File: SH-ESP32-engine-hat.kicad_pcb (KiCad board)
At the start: 2 copper layers, 34 x 58 mm, 66 parts, among them J301 I2C_top, J302 I2C_bottom, J303 GPIO subset, J304 Opto_bottom, J305 1-Wire_top, J306 1-Wire_bottom, J307 Opto_top, J401 Conn_01x02, J402 Conn_01x02, J501 Conn_01x02, J601 Alarm input, Q401 S9015, Q402 S9015, U401 LMV324, U402 RCLAMP0524P-N, U403 RCLAMP0524P-N, U601 ELQ3H7

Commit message: Make all TH headers virtual
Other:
- board text added: "JLCJLCJLCJLC"

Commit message: Fix the footprint for ELQ3H7
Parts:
- U601: footprint Package_SO:SOIC-16W_5.3x10.2mm_P1.27mm -> Package_SO:SOIC-16_4.55x10.3mm_P1.27mm
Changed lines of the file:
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@@
     (add_net "Net-(D603-Pad1)")
     (add_net "Net-(D604-Pad1)")
+    (add_net "Net-(J303-Pad1)")
+    (add_net "Net-(J303-Pad11)")
+    (add_net "Net-(J303-Pad13)")
+    (add_net "Net-(J303-Pad3)")
+    (add_net "Net-(J303-Pad5)")
+    (add_net "Net-(J303-Pad7)")
     (add_net "Net-(J501-Pad2)")
     (add_net "Net-(Q401-Pad1)")
@@
     (add_net "Net-(Q402-Pad1)")
     (add_net "Net-(Q402-Pad2)")
-  )
-  (module SH-ESP32-tank-hat:HL_pictogram_6.3mm (layer F.Cu)
+    (add_net "Net-(U401-Pad14)")
+    (add_net "Net-(U401-Pad8)")
+    (add_net "Net-(U402-Pad2)")
+    (add_net "Net-(U402-Pad4)")
+    (add_net "Net-(U402-Pad5)")
+    (add_net "Net-(U402-Pad6)")
+    (add_net "Net-(U402-Pad7)")
+    (add_net "Net-(U402-Pad9)")
+    (add_net "Net-(U403-Pad2)")
+    (add_net "Net-(U403-Pad4)")
+    (add_net "Net-(U403-Pad5)")
+    (add_net "Net-(U403-Pad6)")
+    (add_net "Net-(U403-Pad7)")
+    (add_net "Net-(U403-Pad9)")
+  )
+  (module Package_SO:SOIC-16_4.55x10.3mm_P1.27mm (layer F.Cu)
+    (at 132.1 73.8 90)
+    (descr "SOIC, 16 Pin (https://toshiba.semicon-storage.com/info/docget.jsp?did=12858&prodName=TLP291-4), generated with kicad-footprint-generator ipc_gullwing_generator.py")
+    (tags "SOIC SO")
+    (attr smd)
+    (fp_text reference U601 (at 0 -6.1 90) (layer F.SilkS) hide
+      (effects (font (size 1 1) (thickness 0.15)))
+    )
+    (fp_text value ELQ3H7 (at 0 6.1 90) (layer F.Fab) hide
+      (effects (font (size 1 1) (thickness 0.15)))
+    )
+    (fp_text user %R (at 0 0 90) (layer F.Fab) hide
+      (effects (font (size 1 1) (thickness 0.15)))
+    )
+    (fp_line (start 0 5.26) (end 2.385 5.26) (layer F.SilkS) (width 0.12))
+    (fp_line (start 2.385 5.26) (end 2.385 4.98) (layer F.SilkS) (width 0.12))
+    (fp_line (start 0 5.26) (end -2.385 5.26) (layer F.SilkS) (width 0.12))
+    (fp_line (start -2.385 5.26) (end -2.385 4.98) (layer F.SilkS) (width 0.12))
+    (fp_line (start 0 -5.26) (end 2.385 -5.26) (layer F.SilkS) (width 0.12))
+    (fp_line (start 2.385 -5.26) (end 2.385 -4.98) (layer F.SilkS) (width 0.12))
+    (fp_line (start 0 -5.26) (end -2.385 -5.26) (layer F.SilkS) (width 0.12))
+    (fp_line (start -2.385 -5.26) (end -2.385 -4.98) (layer F.SilkS) (width 0.12))
+    (fp_line (start -2.385 -4.98) (end -4.05 -4.98) (layer F.SilkS) (width 0.12))
+    (fp_line (start -1.275 -5.15) (end 2.275 -5.15) (layer F.Fab) (width 0.1))
+    (fp_line (start 2.275 -5.15) (end 2.275 5.15) (layer F.Fab) (width 0.1))
+    (fp_line (start 2.275 5.15) (end -2.275 5.15) (layer F.Fab) (width 0.1))
+    (fp_line (start -2.275 5.15) (end -2.275 -4.15) (layer F.Fab) (width 0.1))
+    (fp_line (start -2.275 -4.15) (end -1.275 -5.15) (layer F.Fab) (width 0.1))
+    (fp_line (start -4.3 -5.4) (end -4.3 5.4) (layer F.CrtYd) (width 0.05))
+    (fp_line (start -4.3 5.4) (end 4.3 5.4) (layer F.CrtYd) (width 0.05))
+    (fp_line (start 4.3 5.4) (end 4.3 -5.4) (layer F.CrtYd) (width 0.05))
+    (fp_line (start 4.3 -5.4) (end -4.3 -5.4) (layer F.CrtYd) (width 0.05))
+    (pad 16 smd roundrect (at 3.25 -4.445 90) (size 1.6 0.55) (layers F.Cu F.Paste F.Mask) (roundrect_rratio 0.25)
+      (net 2 +3V3))
+    (pad 15 smd roundrect (at 3.25 -3.175 90) (size 1.6 0.55) (layers F.Cu F.Paste F.Mask) (roundrect_rratio 0.25)
+      (net 38 /AL1))
+    (pad 14 smd roundrect (at 3.25 -1.905 90) (size 1.6 0.55) (layers F.Cu F.Paste F.Mask) (roundrect_rratio 0.25)
+      (net 2 +3V3))
+    (pad 13 smd roundrect (at 3.25 -0.635 90) (size 1.6 0.55) (layers F.Cu F.Paste F.Mask) (roundrect_rratio 0.25)
+      (net 37 /AL2))
+    (pad 12 smd roundrect (at 3.25 0.635 90) (size 1.6 0.55) (layers F.Cu F.Paste F.Mask) (roundrect_rratio 0.25)
+      (net 2 +3V3))
+    (pad 11 smd roundrect (at 3.25 1.905 90) (size 1.6 0.55) (layers F.Cu F.Paste F.Mask) (roundrect_rratio 0.25)
+      (net 36 /AL3))
+    (pad 10 smd roundrect (at 3.25 3.175 90) (size 1.6 0.55) (layers F.Cu F.Paste F.Mask) (roundrect_rratio 0.25)
+      (net 2 +3V3))
+    (pad 9 smd roundrect (at 3.25 4.445 90) (size 1.6 0.55) (layers F.Cu F.Paste F.Mask) (roundrect_rratio 0.25)
+      (net 35 /AL4))
+    (pad 8 smd roundrect (at -3.25 4.445 90) (size 1.6 0.55) (layers F.Cu F.Paste F.Mask) (roundrect_rratio 0.25)
+      (net 29 "/Optocoupler input/GND4"))
+    (pad 7 smd roundrect (at -3.25 3.175 90) (size 1.6 0.55) (layers F.Cu F.Paste F.Mask) (roundrect_rratio 0.25)
+      (net 27 "Net-(D604-Pad1)"))
+    (pad 6 smd roundrect (at -3.25 1.905 90) (size 1.6 0.55) (layers F.Cu F.Paste F.Mask) (roundrect_rratio 0.25)
+      (net 30 "/Optocoupler input/GND3"))
+    (pad 5 smd roundrect (at -3.25 0.635 90) (size 1.6 0.55) (layers F.Cu F.Paste F.Mask) (roundrect_rratio 0.25)
+      (net 25 "Net-(D603-Pad1)"))
+    (pad 4 smd roundrect (at -3.25 -0.635 90) (size 1.6 0.55) (layers F.Cu F.Paste F.Mask) (roundrect_rratio 0.25)
+      (net 31 "/Optocoupler input/GND2"))
+    (pad 3 smd roundrect (at -3.25 -1.905 90) (size 1.6 0.55) (layers F.Cu F.Paste F.Mask) (roundrect_rratio 0.25)
+      (net 23 "Net-(D602-Pad1)"))
+    (pad 2 smd roundrect (at -3.25 -3.175 90) (size 1.6 0.55) (layers F.Cu F.Paste F.Mask) (roundrect_rratio 0.25)
+      (net 32 "/Optocoupler input/GND1"))
+    (pad 1 smd roundrect (at -3.25 -4.445 90) (size 1.6 0.55) (layers F.Cu F.Paste F.Mask) (roundrect_rratio 0.25)
+      (net 21 "Net-(D601-Pad1)"))
+    (model ${KISYS3DMOD}/Package_SO.3dshapes/SOIC-16_4.55x10.3mm_P1.27mm.wrl
+      (at (xyz 0 0 0))
+      (scale (xyz 1 1 1))
+      (rotate (xyz 0 0 0))
+    )
+  )
+  (module SH-ESP32-tank-hat:HL_pictogram_6.3mm locked (layer F.Cu)
     (at 145.2 94.7)
     (fp_text reference G*** (at 0 0) (layer F.SilkS) hide
@@
       (xy -0.095909 -3.166816) (xy 0.183489 -3.163253)) (layer F.SilkS) (width 0.01))
   )
-  (module SH-ESP32-tank-hat:Hat_Labs_20mm (layer B.Cu)
+  (module SH-ESP32-tank-hat:Hat_Labs_20mm locked (layer B.Cu)
     (at 149.3 94.9 180)
     (fp_text reference G*** (at 0 0) (layer B.SilkS) hide
@@
       (at (xyz 0 0 0))
       (scale (xyz 1 1 1))
-      (rotate (xyz 0 0 0))
-    )
-  )
-  (module Package_SO:SOIC-16W_5.3x10.2mm_P1.27mm (layer F.Cu)
-    (at 132.1 73.8 90)
-    (descr "16-Lead Plastic Small Outline (SO) - Wide, 5.3 mm Body (http://www.ti.com/lit/ml/msop002a/msop002a.pdf)")
-    (tags "SOIC 1.27")
-    (attr smd)
-    (fp_text reference U601 (at 0 -6.2 90) (layer F.SilkS) hide
-      (effects (font (size 1 1) (thickness 0.15)))
-    )
-    (fp_text value ELQ3H7 (at 0 6.2 90) (layer F.Fab) hide
-      (effects (font (size 1 1) (thickness 0.15)))
-    )
-    (fp_line (start -2.775 -5) (end -4.3 -5) (layer F.SilkS) (width 0.15))
-    (fp_line (start -2.775 5.275) (end 2.775 5.275) (layer F.SilkS) (width 0.15))
-    (fp_line (start -2.775 -5.275) (end 2.775 -5.275) (layer F.SilkS) (width 0.15))
-    (fp_line (start -2.775 5.275) (end -2.775 4.92) (layer F.SilkS) (width 0.15))
-    (fp_line (start 2.775 5.275) (end 2.775 4.92) (layer F.SilkS) (width 0.15))
-    (fp_line (start 2.775 -5.275) (end 2.775 -4.92) (layer F.SilkS) (width 0.15))
-    (fp_line (start -2.775 -5.275) (end -2.775 -5) (layer F.SilkS) (width 0.15))
-    (fp_line (start -4.55 5.45) (end 4.55 5.45) (layer F.CrtYd) (width 0.05))
-    (fp_line (start -4.55 -5.45) (end 4.55 -5.45) (layer F.CrtYd) (width 0.05))
-    (fp_line (start 4.55 -5.45) (end 4.55 5.45) (layer F.CrtYd) (width 0.05))
-    (fp_line (start -4.55 -5.45) (end -4.55 5.45) (layer F.CrtYd) (width 0.05))
-    (fp_line (start -2.65 -4.1) (end -1.65 -5.1) (layer F.Fab) (width 0.15))
-    (fp_line (start -2.65 5.1) (end -2.65 -4.1) (layer F.Fab) (width 0.15))
-    (fp_line (start 2.65 5.1) (end -2.65 5.1) (layer F.Fab) (width 0.15))
-    (fp_line (start 2.65 -5.1) (end 2.65 5.1) (layer F.Fab) (width 0.15))
-    (fp_line (start -1.65 -5.1) (end 2.65 -5.1) (layer F.Fab) (width 0.15))
-    (fp_text user %R (at 0 0 90) (layer F.Fab) hide
-      (effects (font (size 1 1) (thickness 0.15)))
-    )
-    (pad 16 smd rect (at 3.55 -4.445 90) (size 1.5 0.6) (layers F.Cu F.Paste F.Mask)
-      (net 2 +3V3))
-    (pad 15 smd rect (at 3.55 -3.175 90) (size 1.5 0.6) (layers F.Cu F.Paste F.Mask)
-      (net 38 /AL1))
-    (pad 14 smd rect (at 3.55 -1.905 90) (size 1.5 0.6) (layers F.Cu F.Paste F.Mask)
-      (net 2 +3V3))
-    (pad 13 smd rect (at 3.55 -0.635 90) (size 1.5 0.6) (layers F.Cu F.Paste F.Mask)
-      (net 37 /AL2))
-    (pad 12 smd rect (at 3.55 0.635 90) (size 1.5 0.6) (layers F.Cu F.Paste F.Mask)
-      (net 2 +3V3))
-    (pad 11 smd rect (at 3.55 1.905 90) (size 1.5 0.6) (layers F.Cu F.Paste F.Mask)
-      (net 36 /AL3))
-    (pad 10 smd rect (at 3.55 3.175 90) (size 1.5 0.6) (layers F.Cu F.Paste F.Mask)
-      (net 2 +3V3))
-    (pad 9 smd rect (at 3.55 4.445 90) (size 1.5 0.6) (layers F.Cu F.Paste F.Mask)
-      (net 35 /AL4))
-    (pad 8 smd rect (at -3.55 4.445 90) (size 1.5 0.6) (layers F.Cu F.Paste F.Mask)
-      (net 29 "/Optocoupler input/GND4"))
-    (pad 7 smd rect (at -3.55 3.175 90) (size 1.5 0.6) (layers F.Cu F.Paste F.Mask)
-      (net 27 "Net-(D604-Pad1)"))
-    (pad 6 smd rect (at -3.55 1.905 90) (size 1.5 0.6) (layers F.Cu F.Paste F.Mask)
-      (net 30 "/Optocoupler input/GND3"))
-    (pad 5 smd rect (at -3.55 0.635 90) (size 1.5 0.6) (layers F.Cu F.Paste F.Mask)
-      (net 25 "Net-(D603-Pad1)"))
-    (pad 4 smd rect (at -3.55 -0.635 90) (size 1.5 0.6) (layers F.Cu F.Paste F.Mask)
-      (net 31 "/Optocoupler input/GND2"))
-    (pad 3 smd rect (at -3.55 -1.905 90) (size 1.5 0.6) (layers F.Cu F.Paste F.Mask)
-      (net 23 "Net-(D602-Pad1)"))
-    (pad 2 smd rect (at -3.55 -3.175 90) (size 1.5 0.6) (layers F.Cu F.Paste F.Mask)
-      (net 32 "/Optocoupler input/GND1"))
-    (pad 1 smd rect (at -3.55 -4.445 90) (size 1.5 0.6) (layers F.Cu F.Paste F.Mask)
-      (net 21 "Net-(D601-Pad1)"))
-    (model ${KISYS3DMOD}/Package_SO.3dshapes/SOIC-16W_5.3x10.2mm_P1.27mm.wrl
-      (at (xyz 0 0 0))
-      (scale (xyz 1 1 1))

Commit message: Fix the wrong LCSC component for R501
Also silkscreen fixes
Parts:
- J307: footprint Connector_PinSocket_2.54mm:PinSocket_1x03_P2.54mm_Vertical -> Connector_PinHeader_2.54mm:PinHeader_1x03_P2.54mm_Vertical

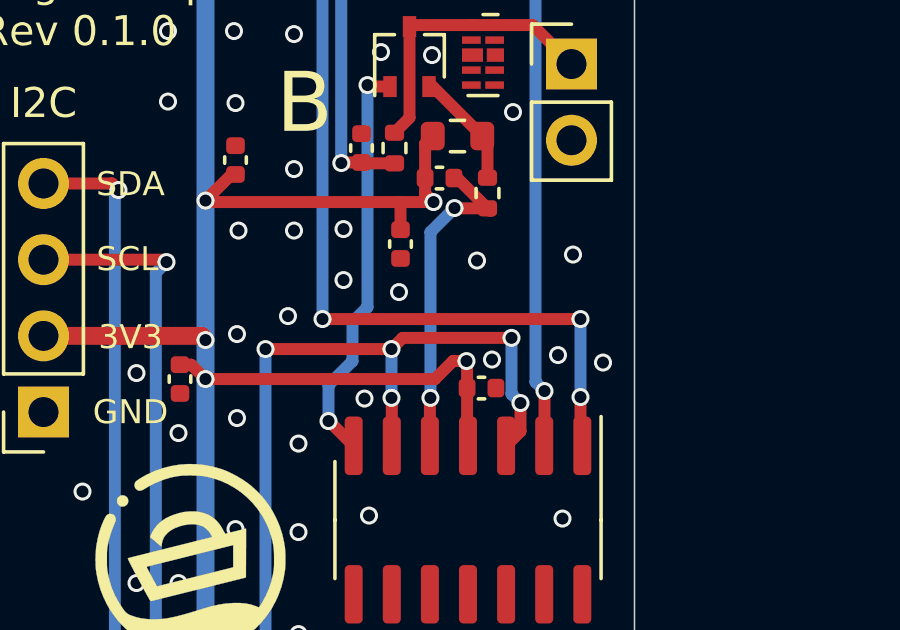
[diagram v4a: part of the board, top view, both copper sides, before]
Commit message: Fix the reversed tank input B opto inputs
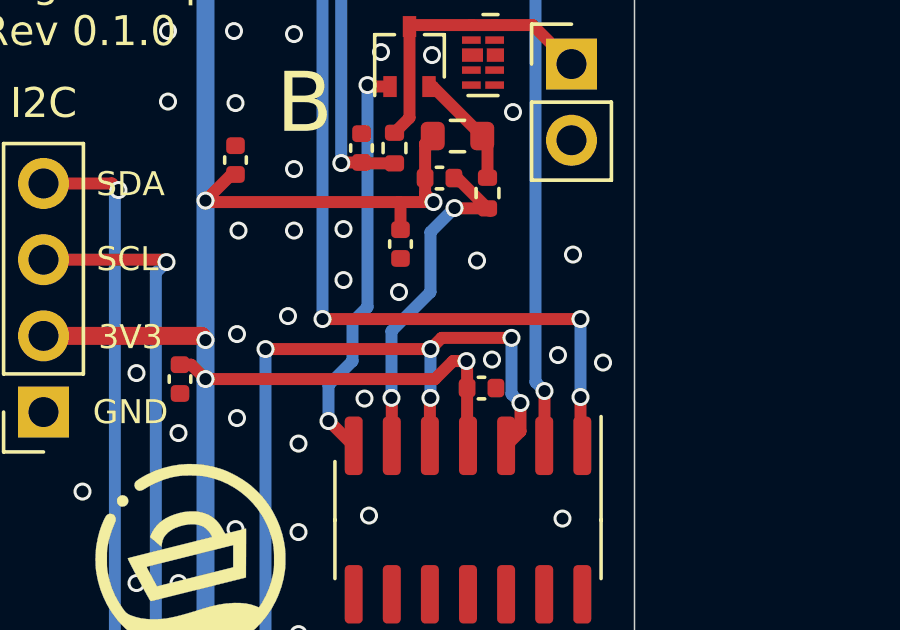
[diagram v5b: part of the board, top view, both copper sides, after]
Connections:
- U401 pad 5: Net-(C402-Pad1) -> /Tank sender/Vin
- U401 pad 6: /Tank sender/Vin -> Net-(C402-Pad1)
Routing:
- net Net-(C402-Pad1): track 11.0 -> 11.6 mm
